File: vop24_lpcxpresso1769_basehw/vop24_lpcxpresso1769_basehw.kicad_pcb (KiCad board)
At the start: 2 copper layers, 105 x 150 mm, 117 parts, among them J1 Micro_SD_Card, J101 Conn_01x03_Male, J2 Conn_01x05_Male, J201 Screw_Terminal_01x02, J3 Conn_01x06_Male, J301 USB_B_Micro, J302 Screw_Terminal_01x02, J401 Conn_01x02, J402 Conn_01x02, J403 Conn_01x02, J404 Conn_01x04, J405 Conn_01x04, J406 Conn_01x04, U1 LPCXpresso1769, U101 MCP1700T-3302E_TT, U102 MCP1700T-3302E_TT, U103 TPS63001, U201 LM358, U301 LTC4411, U302 TPD4S014, U303 LT1512, U401 ADS1292, U402 LM334, U403 LM334, U404 LM334

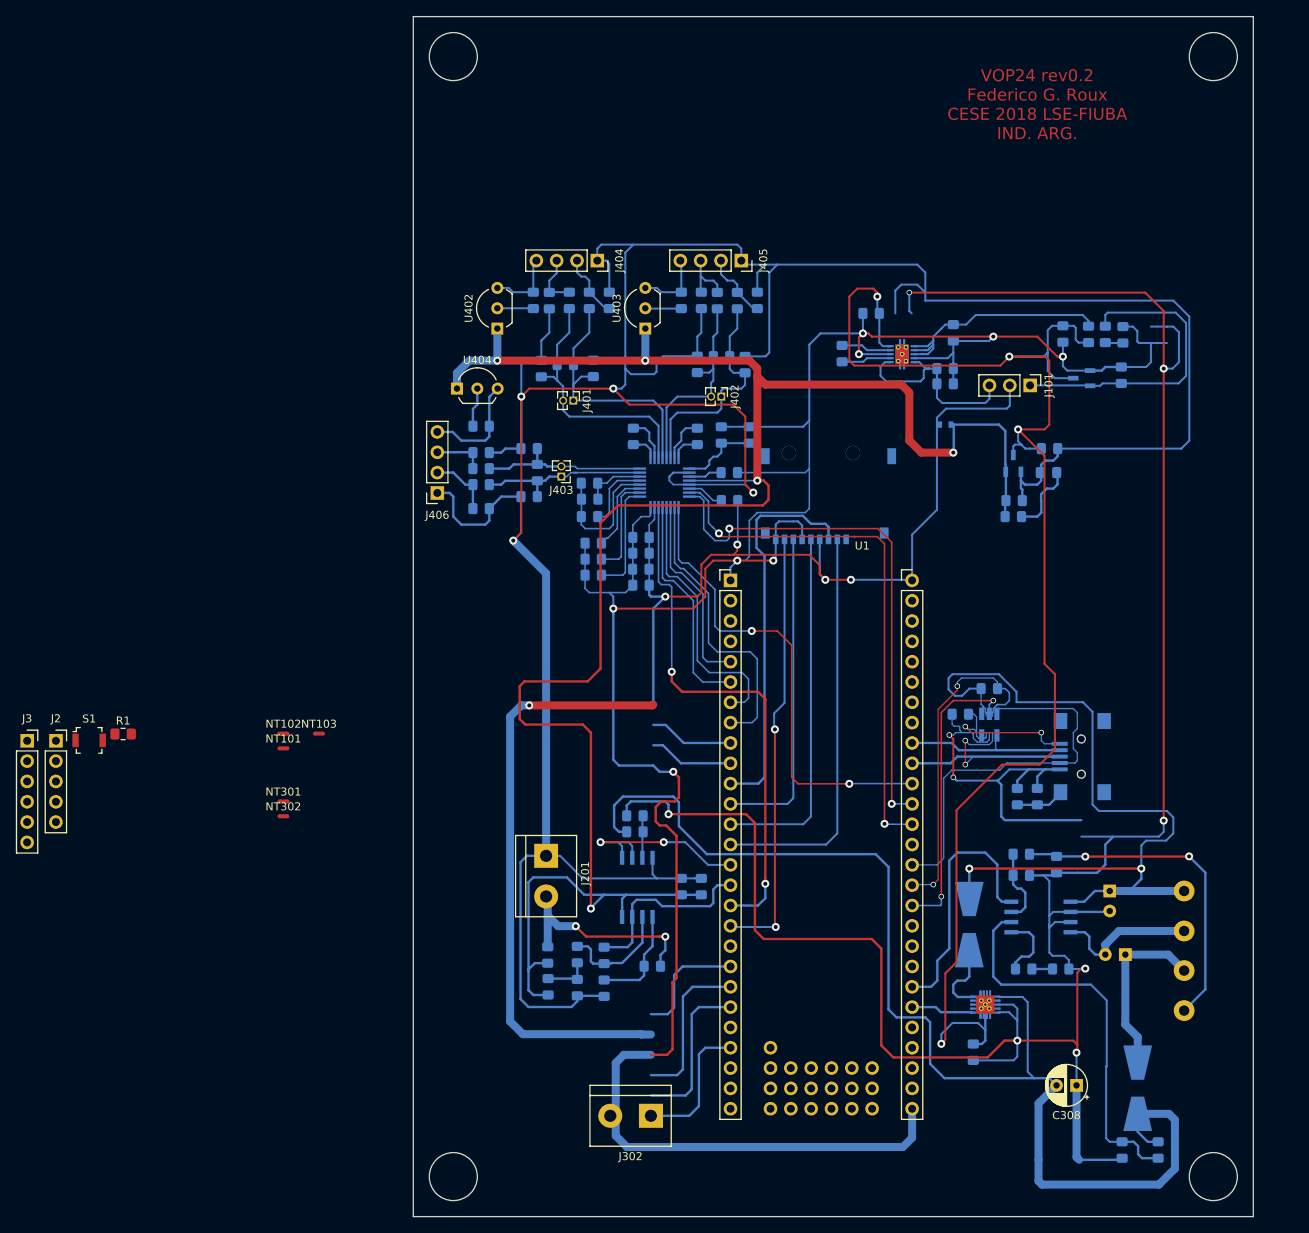
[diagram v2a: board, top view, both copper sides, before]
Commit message: ESQ: cambios en net-tie y footprints PCB: cambios grandes de dimensiones y ruteo
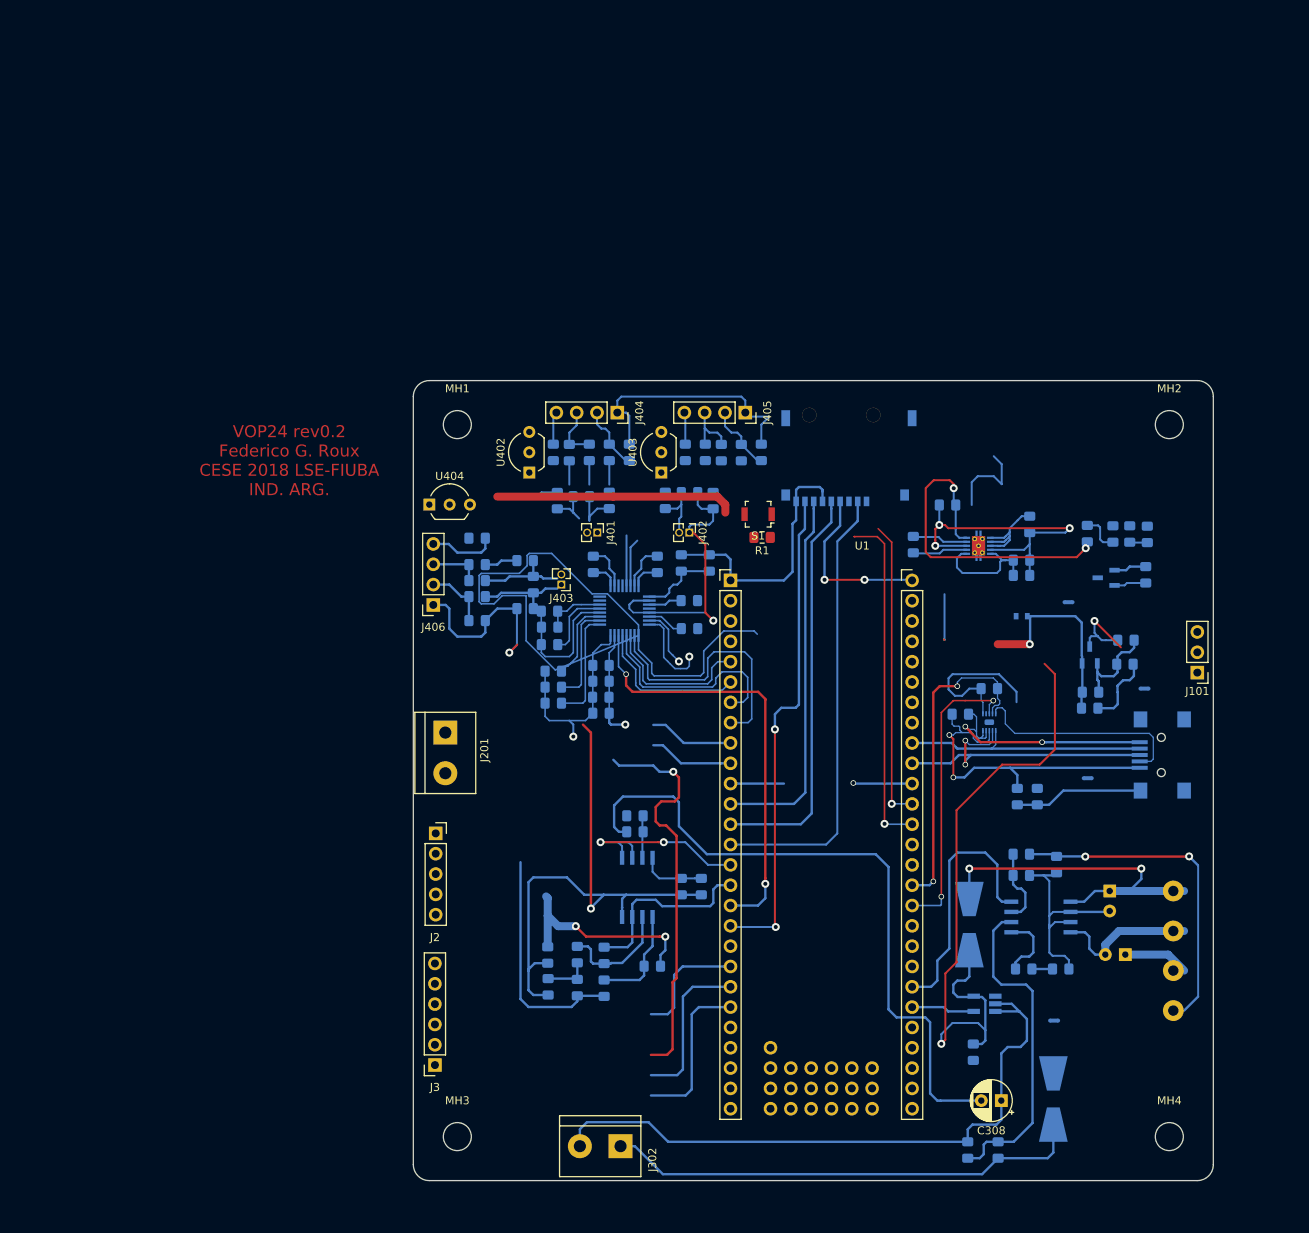
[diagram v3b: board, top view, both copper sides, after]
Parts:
- removed NT101: Net-Tie_2, NetTie:NetTie-2_SMD_Pad0.5mm
- added MH1: MountingHole, MountingHole:MountingHole_3.5mm, F.Cu at (45.5, 86.0)
- added MH2: MountingHole, MountingHole:MountingHole_3.5mm, F.Cu at (134.5, 86.0)
- added MH3: MountingHole, MountingHole:MountingHole_3.5mm, F.Cu at (45.5, 175.0)
- added MH4: MountingHole, MountingHole:MountingHole_3.5mm, F.Cu at (134.5, 175.0)
- NT102, NT103, NT301, NT302: moved to B.Cu
- U302: footprint Package_SON:Texas_S-PWSON-N10_ThermalVias -> meport_kicad_libs:Texas_R-PWSON-N10
- moved NT103 103.3 mm to (131.4, 119.0)
- moved NT302 100.7 mm to (124.3, 130.2)
- moved NT301 100.2 mm to (120.1, 160.5), turned to 180 degrees
- moved NT102 99.5 mm to (121.9, 108.2)
- moved S1 88.3 mm to (83.1, 97.2), turned to 180 degrees
- moved R1 83.6 mm to (83.6, 100.1), turned to 180 degrees
- moved J3 65.1 mm to (42.7, 166.1), turned to 180 degrees
- moved J2 48.9 mm to (42.8, 137.1)
- moved J101 41.5 mm to (138.0, 117.0), turned to 180 degrees
- moved U302 35.3 mm to (112.0, 123.2), turned to 270 degrees
- moved U301 34.9 mm to (111.4, 158.4), turned to 180 degrees
- moved C103 25.8 mm to (106.8, 96.0)
- moved C106 25.8 mm to (124.7, 119.5)
- moved C107 25.8 mm to (116.0, 103.0)
- moved U103 25.8 mm to (110.7, 101.2)
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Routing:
- net /analogico/GNDBAT: track 296.6 -> 0.00 mm, vias 7 -> 0
- net GNDA: track 414.5 -> 151.9 mm, vias 4 -> 2
- net /fuentesLDO/VCC_NREG: track 191.4 -> 0.00 mm, vias 4 -> 0
- net GNDD: track 326.4 -> 154.7 mm, vias 8 -> 5
- net /analogico/VBAT: track 151.5 -> 0.00 mm
- net +BATT: track 0.00 -> 144.2 mm
- net VDDA: track 261.9 -> 125.6 mm, vias 5 -> 2
- net VCOM: track 7.49 -> 128.1 mm, vias 0 -> 3
- net -BATT: track 0.00 -> 109.2 mm
- net /VUSB_OUT: track 107.4 -> 0.00 mm, vias 2 -> 0
- net /DVCC: track 74.9 -> 0.00 mm, vias 1 -> 0
- net VDD: track 110.8 -> 40.6 mm, vias 4 -> 3
- net VBUS: track 0.00 -> 63.8 mm, vias 0 -> 2
- net /MOSI_SD: track 48.5 -> 6.67 mm
- net /fuentesLDO/DVCC_LDO: track 38.9 -> 4.09 mm
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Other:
- board size 105 x 150 mm -> 100 x 100 mm
- board text added: "Notas ancho de pistas, vías y agujero de vía (mín): Ancho de pista: 0.2 mm Agujero: 0.4 mm Vias: 0.8 mm"
- board text added: "Notas de Grilla: Grilla : 0,1 mm Margen : 0,2 mm"
- board text removed: "Notas de Grilla: Grid: 0,1mm"

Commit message: ESQ: cambios menores PCB: finalizacion de ruteo con 0.3mm. Previo a poligonos
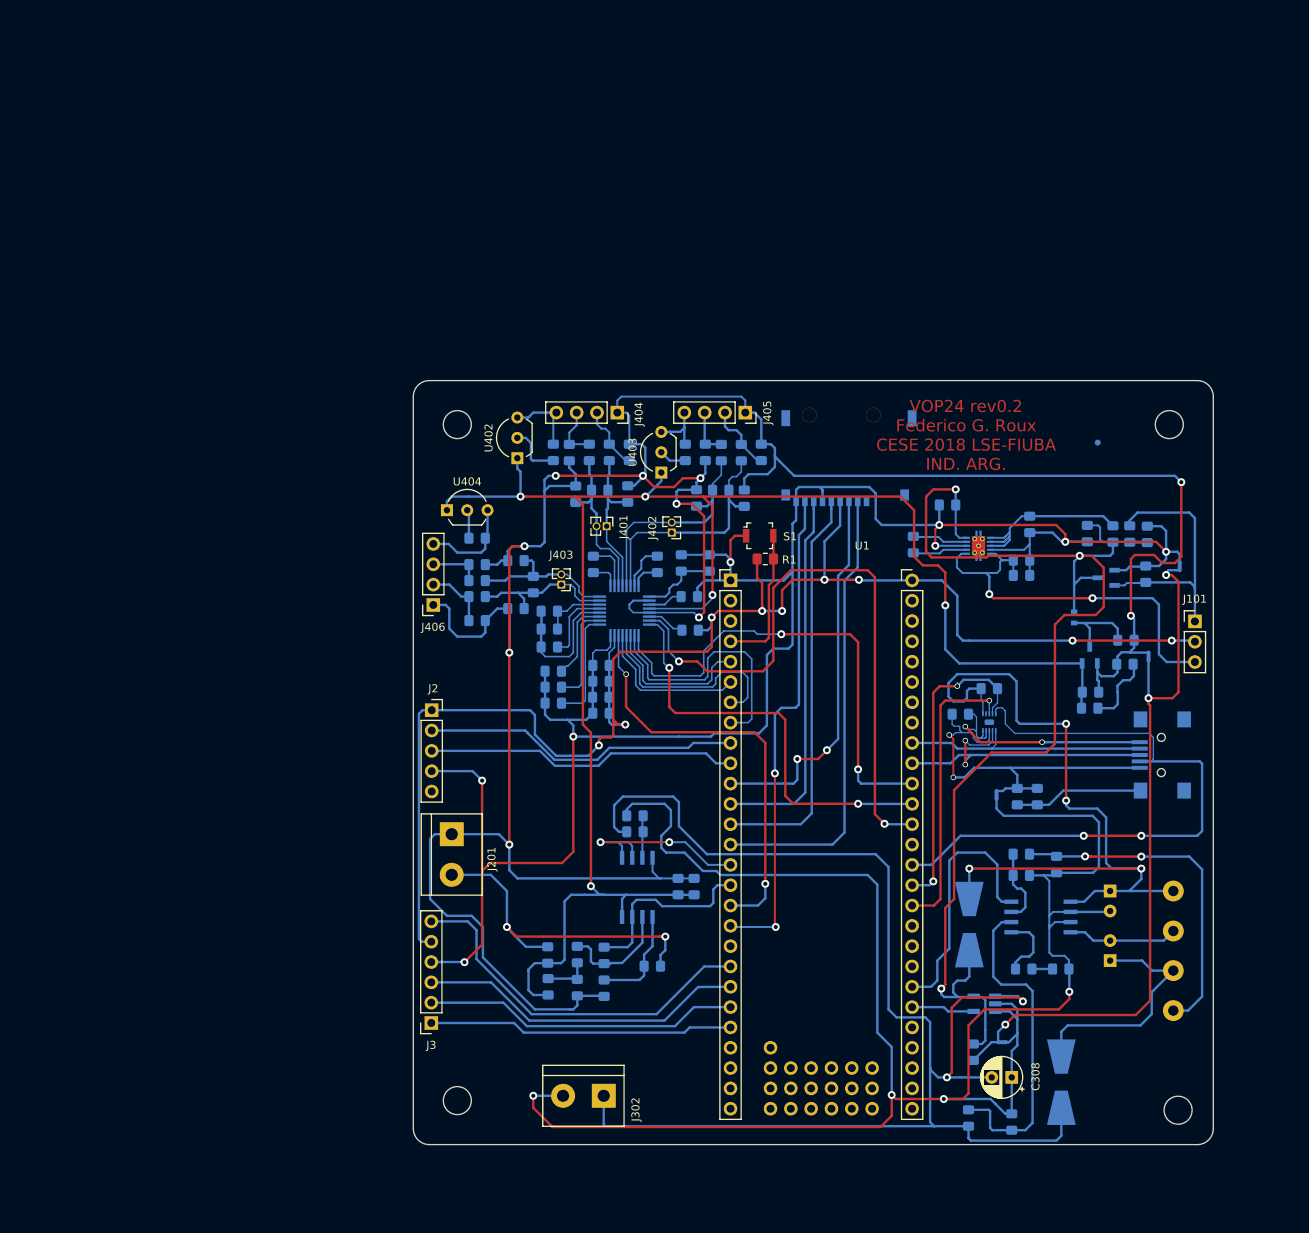
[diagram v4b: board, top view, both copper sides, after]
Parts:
- added FIDBACK1: MountingHole, Fiducial:Fiducial_0.75mm_Dia_1.5mm_Outer, B.Cu at (125.5, 88.2)
- moved J2 15.4 mm to (42.3, 121.7)
- moved NT102 14.6 mm to (135.8, 103.7), turned to 90 degrees
- moved J201 12.7 mm to (44.8, 137.2)
- moved NT302 11.6 mm to (112.9, 132.3), turned to 270 degrees
- moved NT301 7.04 mm to (113.6, 163.2)
- moved J302 6.64 mm to (63.8, 169.9)
- moved FB101 6.55 mm to (122.6, 110.1), turned to 270 degrees
- moved R308 6.52 mm to (114.8, 173.2)
- moved J101 6.41 mm to (137.7, 110.6), turned to 0 degrees
- moved R307 5.45 mm to (109.4, 172.7)
- moved J3 5.28 mm to (42.2, 160.8)
- moved MH3 4.50 mm to (45.5, 170.5)
- moved NT103 4.03 mm to (131.9, 115.0), turned to 90 degrees
- moved C417 3.91 mm to (75.4, 95.2)
- moved C418 3.91 mm to (81.4, 95.2)
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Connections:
- U1 pad 54: GNDD -> Net-(U1-Pad54)
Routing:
- net GNDA: track 151.9 -> 364.6 mm, vias 2 -> 10
- net VDD: track 40.6 -> 191.4 mm, vias 3 -> 9
- net -BATT: track 109.2 -> 243.8 mm, vias 0 -> 4
- net GNDD: track 154.7 -> 270.3 mm, vias 5 -> 8
- net VDDA: track 125.6 -> 223.2 mm, vias 2 -> 5
- net GNDREF: track 0.00 -> 90.6 mm, vias 0 -> 3
- net /USB_ID: track 27.3 -> 80.3 mm, vias 0 -> 2
- net /MOSI_SD: track 6.67 -> 47.5 mm, vias 0 -> 2
- net /BLE_STATE: track 0.00 -> 38.3 mm
- net /fuentesLDO/DVCC_UD: track 15.3 -> 51.0 mm, vias 0 -> 2
- net VBUS: track 63.8 -> 99.4 mm, vias 2 -> 4
- net +BATT: track 144.2 -> 178.8 mm, vias 0 -> 2
- net /BLE_EN: track 14.8 -> 46.9 mm
- net /UUTXD: track 10.6 -> 39.9 mm
- net /fuentesLDO/DVCC_LDO: track 4.09 -> 33.2 mm
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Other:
- board size 100 x 100 mm -> 100 x 95.5 mm
- net class Default: clearance 0.1 -> 0.2
- net class mayer8mils: clearance 0.1 -> 0.2
- rule trace_clearance: 0.1 -> 0.2
- board text added: "NOTAS DE FABRICACION: Este prototipo está diseñado para ser fabricado en un CNC Router para probar las conexiones de cada uno de los módulos. Por ello se usó un solo lado para soldar componentes y minimizar la cantidad de vías. Los componentes SMD están sobre la capa inferior porque es como físicamente queda ubicada. Los componentes Through- Hole están sobre la capa superior para que la conexión 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"
- board text added: "TAMAÑO DE PISTAS, VIAS y CLEARANCE: Se crearon las Reglas de Diseño de acuerdo a los estándares de Mayer de 12-10-8-6 mils que se vieron en la cátedra. La mayor parte de la placa está resuelta en el estándar de 12 mils, y en donde se puede, se usaron pistas más grandes. Solo para los componentes ADS1292 y TPD4S se usaron pistas mas finas (10 y 8 mils respectivamente)"
- board text removed: "NOTA SERIGRAFÍA: Como se menciona más arriba, este primer diseño es para realizar en un ROUTER CNC, por lo que no se le dió mucha importancia a la capa de serigrafía porque no se va a realizar. En el diseño final se ubicarán las leyendas de los componentes de una forma más prolija."
- board text removed: "NOTA UBICACIÓN COMPONENTES: Los componentes están agrupados por módulo para poder que sea más fácil la inspección a la hora de hacer pruebas, ya que se trata de un prototipo. Además, el hecho de trabajar alrededor de un LPCXpresso hace que el diseño sea más limitado y de mucho mayor tamaño que lo que debería ocupar."
- board text removed: "NOTAS CONECTORES: Los conectores J301 y J302 son tiras de pines para conectar directamente los modulos UART-TTL y UART-BLE. No se ubican sobre el borde para que no sobresalgan estas placas hacia afuera, o sobresalgan lo menos posible. El conector miniUSB se ubica lo más cerca del LPCXpresso posible, ya que la conexión no es directa sino a través del STICK, y eso complica la señal de alta velocida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"
- board text removed: "NOTAS DE FABRICACION: Este prototipo está diseñado para ser fabricado en un CNC Router para probar las conexiones de cada uno de los módulos. Por ello se usó un solo lado para soldar componentes y minimizar la cantidad de vías. En el siguiente diseño se hará para fabricar en Mayer o Inarci, y se colocará el microcontrolador en lugar del LPCXpresso"
- board text removed: "NOTAS DRC: Solamente se marcan los pines no conectados del SHIELD del conector USB, que están cortocircuitados internamente"
- board text removed: "TAMAÑO DE PISTAS, VIAS y CLEARANCE: Se crearon las Reglas de Diseño de acuerdo a los estándares de Mayer de 12-10-8-6 mils que se vieron en la cátedra. La mayor parte de la placa está resuelta en el estándar de 8 mils, y en donde se puede, se usaron pistas más grandes."

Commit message: Version entregada 2
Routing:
- added copper zone on B.Cu, net GNDA
- added copper zone on F.Cu, net GNDD
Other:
- board text added: "NOTAS DE FABRICACION: Este prototipo está diseñado para ser fabricado en un CNC Router para probar las conexiones de cada uno de los módulos. La resolución es similar a Mayer, pero sin poder realizar agujeros metalizados de forma cómoda, se hace un agujero y se suelda un alambre de ambos lados. Por ello se usó un solo lado para soldar componentes y minimizar la cantidad de vías. Los componentes S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"
- board text added: "NOTAS TERMINACION SUPERFICIAL: Se realiza con capa de máscara antisoldante, serifrafía y mascara soldante."
- board text removed: "NOTAS DE FABRICACION: Este prototipo está diseñado para ser fabricado en un CNC Router para probar las conexiones de cada uno de los módulos. Por ello se usó un solo lado para soldar componentes y minimizar la cantidad de vías. Los componentes SMD están sobre la capa inferior porque es como físicamente queda ubicada. Los componentes Through- Hole están sobre la capa superior para que la conexión 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"
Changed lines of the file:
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@@
   (general
     (thickness 1.6)
-    (drawings 15)
-    (tracks 1377)
+    (drawings 16)
+    (tracks 1376)
     (zones 0)
     (modules 121)
@@
   )
   (setup
-    (last_trace_width 0.25)
+    (last_trace_width 0.2)
     (user_trace_width 0.15)
     (user_trace_width 0.2)
@@
     )
   )
+  (gr_text "NOTAS TERMINACION SUPERFICIAL:\nSe realiza con capa de máscara antisoldante, serifrafía y mascara soldante." (at 225 110) (layer Eco1.User)
+    (effects (font (size 1.5 1.5) (thickness 0.3)))
+  )
   (gr_text "VOP24 rev0.2\nFederico G. Roux\nCESE 2018 LSE-FIUBA\nIND. ARG." (at 109.1 87.35) (layer F.Cu)
     (effects (font (size 1.5 1.5) (thickness 0.3)))
@@
     (effects (font (size 1.5 1.5) (thickness 0.3)) (justify left))
   )
-  (gr_text "NOTAS DE FABRICACION:\nEste prototipo está diseñado para ser fabricado en un CNC Router para \nprobar las conexiones de cada uno de los módulos. \n\nPor ello se usó un solo lado para soldar componentes y minimizar la\ncantidad de vías. Los componentes SMD están sobre la capa inferior\nporque es como físicamente queda ubicada. Los componentes Through-\nHole están sobre la capa superior para que la conexión quede del lado\ninferior.\n\n\nEn el siguiente diseño se hará para fabricar en Mayer o Inarci, y se\ncolocará el microcontrolador en lugar del LPCXpresso" (at 225.45 82.45) (layer Eco1.User)
+  (gr_text "NOTAS DE FABRICACION:\nEste prototipo está diseñado para ser fabricado en un CNC Router para \nprobar las conexiones de cada uno de los módulos.  La resolución es \nsimilar a Mayer, pero sin poder realizar agujeros metalizados de forma\ncómoda, se hace un agujero y se suelda un alambre de ambos lados.\n\nPor ello se usó un solo lado para soldar componentes y minimizar la\ncantidad de vías. Los componentes SMD están sobre la capa inferior\nporque es como físicamente queda ubicada. Los componentes Through-\nHole están sobre la capa superior para que la conexión quede del lado\ninferior.\n\n\nEn el siguiente diseño se hará para fabricar en Mayer o Inarci, y se\ncolocará el microcontrolador en lugar del LPCXpresso" (at 225.45 82.45) (layer Eco1.User)
     (effects (font (size 1.5 1.5) (thickness 0.3)))
   )
@@
   (segment (start 55.9 101.2) (end 53.9 101.2) (width 0.3) (layer B.Cu) (net 125))
   (segment (start 53.9 101.2) (end 52.4 101.2) (width 0.3) (layer B.Cu) (net 125))
-  (segment (start 69.5 108.5) (end 71.5 108.5) (width 0.25) (layer B.Cu) (net 126))
-  (segment (start 71.5 108.5) (end 71.5 108.4) (width 0.2) (layer B.Cu) (net 126))
-  (segment (start 72.4 107.5) (end 73.475 107.5) (width 0.2) (layer B.Cu) (net 126))
-  (segment (start 71.5 108.4) (end 72.4 107.5) (width 0.2) (layer B.Cu) (net 126))
+  (segment (start 71.4 108.5) (end 69.5 108.5) (width 0.2) (layer B.Cu) (net 126))
+  (segment (start 72.4 107.5) (end 71.4 108.5) (width 0.2) (layer B.Cu) (net 126))
+  (segment (start 73.475 107.5) (end 72.4 107.5) (width 0.2) (layer B.Cu) (net 126))
   (segment (start 59.144541 116.197119) (end 58.521169 116.820491) (width 0.2) (layer B.Cu) (net 127))
   (segment (start 59.302881 116.197119) (end 59.144541 116.197119) (width 0.2) (layer B.Cu) (net 127))
@@
   (segment (start 134.9 120.2) (end 131.9 120.2) (width 0.3) (layer F.Cu) (net 136))
   (segment (start 135.650001 119.449999) (end 134.9 120.2) (width 0.3) (layer F.Cu) (net 136))
+  (zone (net 125) (net_name GNDA) (layer B.Cu) (hatch edge 0.508)
+    (connect_pads (clearance 0.508))
+    (min_thickness 0.254)
+    (fill yes (arc_segments 16) (thermal_gap 0.508) (thermal_bridge_width 0.508))
+    (polygon
+      (pts
+        (xy 35 75) (xy 145 75) (xy 145 180) (xy 35 180)
+      )
+    )
+  )
+  (zone (net 120) (net_name GNDD) (layer F.Cu) (hatch edge 0.508)
+    (connect_pads (clearance 0.508))
+    (min_thickness 0.254)
+    (fill yes (arc_segments 16) (thermal_gap 0.508) (thermal_bridge_width 0.508))
+    (polygon
+      (pts
+        (xy 30 185) (xy 30 70) (xy 150 70) (xy 150 185)
+      )
+    )
+  )
 )
